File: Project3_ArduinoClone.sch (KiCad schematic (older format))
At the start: 13 parts, among them U1 24LC1025, U2 24LC1025, U3 DS1337_v1, U4 ATMEGA328P-AU, Y1 Crystal 32 MHz, Y2 Crystal 16 MHz

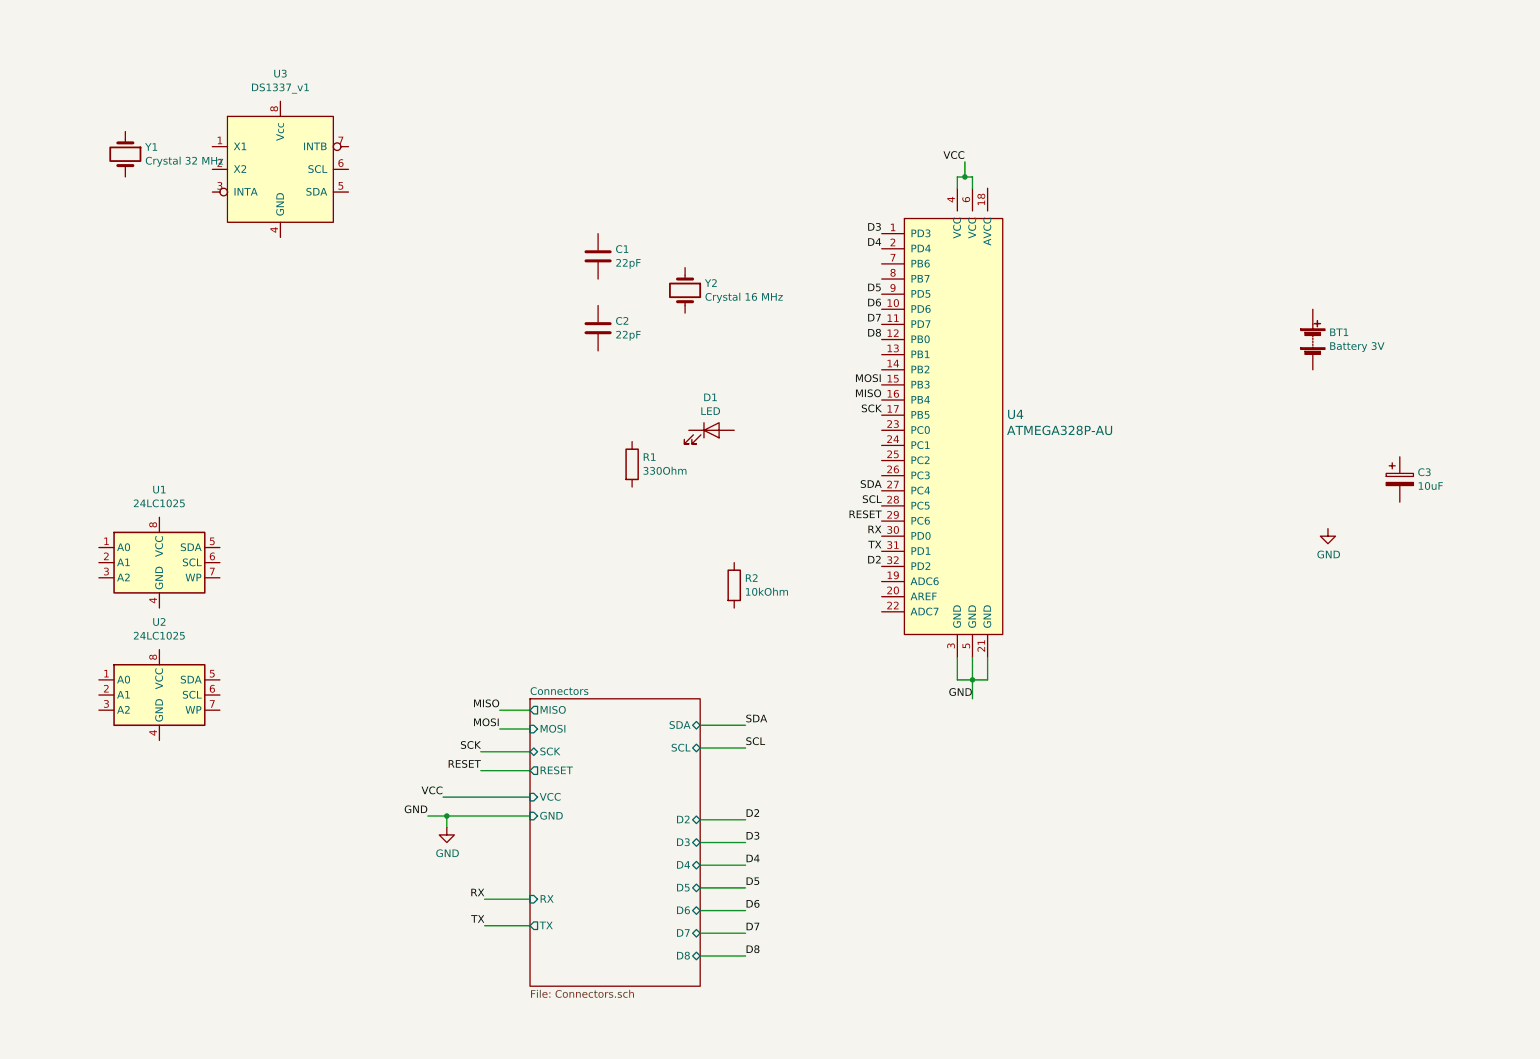
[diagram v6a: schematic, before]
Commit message: Wire entire root sheet
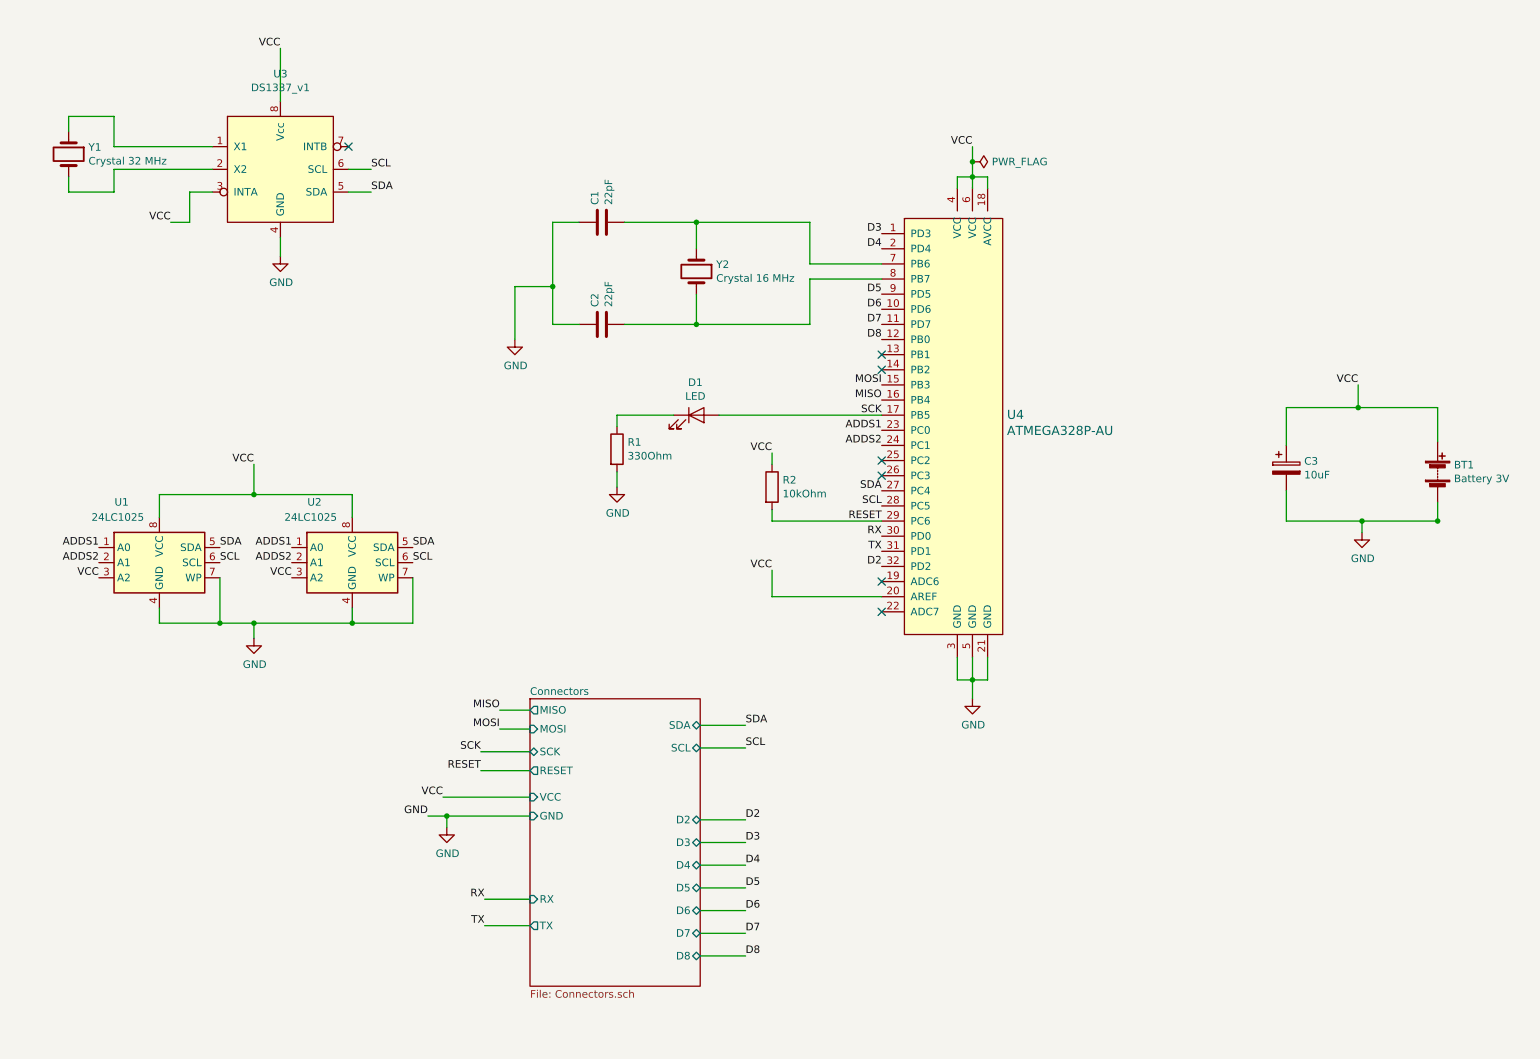
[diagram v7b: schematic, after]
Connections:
- net GND: now also BT1.2 (-), C1.1, C2.1, C3.2, R1.2, U1.4 (GND), U1.7 (WP), U2.4 (GND), U2.7 (WP), U3.4 (GND)
- net RESET: now also R2.2
- net SCK: now also D1.2 (A)
- net SCL: now also U1.6 (SCL), U2.6 (SCL), U3.6 (SCL)
- net SDA: now also U1.5 (SDA), U2.5 (SDA), U3.5 (SDA)
- net VCC: now also BT1.1 (+), C3.1, R2.1, U1.3 (A2), U1.8 (VCC), U2.3 (A2), U2.8 (VCC), U3.3 (INTA), U3.8 (Vcc), U4.18 (AVCC), U4.20 (AREF)
- net at C1.2: now also U4.7 (PB6), Y2.1
- net at C2.2: now also U4.8 (PB7), Y2.2
- net at D1.1 (K): now also R1.1
- net ADDS1: now reaches U4.23 (PC0)
- net ADDS1: now also U1.1 (A0), U2.1 (A0)
- net ADDS2: now reaches U4.24 (PC1)
- net ADDS2: now also U1.2 (A1), U2.2 (A1)
- net at U3.1 (X1): now also Y1.1
- net at U3.2 (X2): now also Y1.2
- no-connect marks 0 -> 7
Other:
- moved on the sheet: BT1, C1, C2, C3, D1, R1, R2, U2, Y1, Y2

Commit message: Comment sections and generate netlist
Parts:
- U3: symbol Pablo_KiCad:DS1337_v1 -> Pablo_Kicad_library:DS1337_v1
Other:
- note added: "N1 - Real Time Clock"
- note added: "N2 - External EEPROMs"
- note added: "N3 - Atmega328P"
- note added: "N4 - Battery"
- note added: "N5 - Connectors sheet"
- moved on the sheet: BT1, C1, C2, C3, D1, R1, R2, U1, U2, U4, Y2
